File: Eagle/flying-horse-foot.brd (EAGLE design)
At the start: 55.8 x 32.5 mm, 20 parts, among them U1 8U2-AU, Y1 16MHz

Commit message: rel 1
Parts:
- added S1: MK6-5-B, switch-reed:MK6-5
- C4, C6: value 0.1uF -> 1.0uF
- C7, C8: value 1.0uF -> 0.1uF
- U$1, U$2: value 74HC42 -> 74HC42D16; device aaa2:SOIC127P1032X265-16N -> aaa2:D16
- moved RESET 36.1 mm to (42.5, 17.1), turned to 270 degrees
- moved C5 23.6 mm to (41.9, 25.4)
- moved C8 22.9 mm to (13.3, 30.7)
- moved C7 20.7 mm to (45.7, 1.91)
- moved C4 18.3 mm to (36.8, 21.0)
- moved C6 8.02 mm to (36.8, 30.9), turned to 180 degrees
- moved C2 4.58 mm to (41.8, 30.9), turned to 180 degrees
- moved C3 2.29 mm to (41.9, 28.6)
- moved R1 2.16 mm to (46.4, 22.6)
- moved R2 1.90 mm to (46.4, 24.8)
- moved U$1 1.80 mm to (45.7, 8.26)
- moved R5 1.65 mm to (4.45, 29.0)
- moved Y1 1.42 mm to (45.7, 29.8), turned to 90 degrees
- moved U$2 1.02 mm to (13.3, 24.4)
- moved C1 0.63 mm to (50.2, 29.2)
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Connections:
- removed net N$9: RESET.2, U1.24
- new net RESET: RESET.2, S1.1, U1.24
- net COL-3: no longer U$4.13
- net COL-5: now also U$4.13
- net GND: now also C5.1, C8.2, S1.2; no longer C5.2, C8.1
- net N$3: now also C2.1; no longer C3.1
- net N$4: now also C3.1; no longer C2.1
- net N$6: now also C4.1; no longer C7.1
- net VCC: now also C5.2, C7.1, C8.1; no longer C4.1, C5.1, C8.2
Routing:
- net VCC: track 0.00 -> 94.5 mm, vias 0 -> 4
- net ROW-A: track 0.00 -> 57.2 mm, vias 0 -> 2
- net ROW-B: track 0.00 -> 55.1 mm, vias 0 -> 2
- net ROW-C: track 0.00 -> 51.5 mm, vias 0 -> 2
- net ROW-D: track 0.00 -> 50.6 mm, vias 0 -> 2
- net ROW-5: track 0.00 -> 41.2 mm, vias 0 -> 2
- net ROW-18: track 0.00 -> 41.0 mm, vias 0 -> 2
- net COL-12: track 0.00 -> 40.6 mm, vias 0 -> 1
- net ROW-17: track 0.00 -> 39.6 mm
- net COL-6: track 0.00 -> 38.2 mm, vias 0 -> 1
- net COL-5: track 0.00 -> 36.3 mm, vias 0 -> 1
- net N$5: track 0.00 -> 32.5 mm, vias 0 -> 2
- net COL-4: track 0.00 -> 31.1 mm, vias 0 -> 1
- net COL-0: track 0.00 -> 29.8 mm, vias 0 -> 1
- net N$7: track 0.00 -> 28.7 mm, vias 0 -> 2
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- added copper zone on layer 1, net GND
- added copper zone on layer 16, net GND

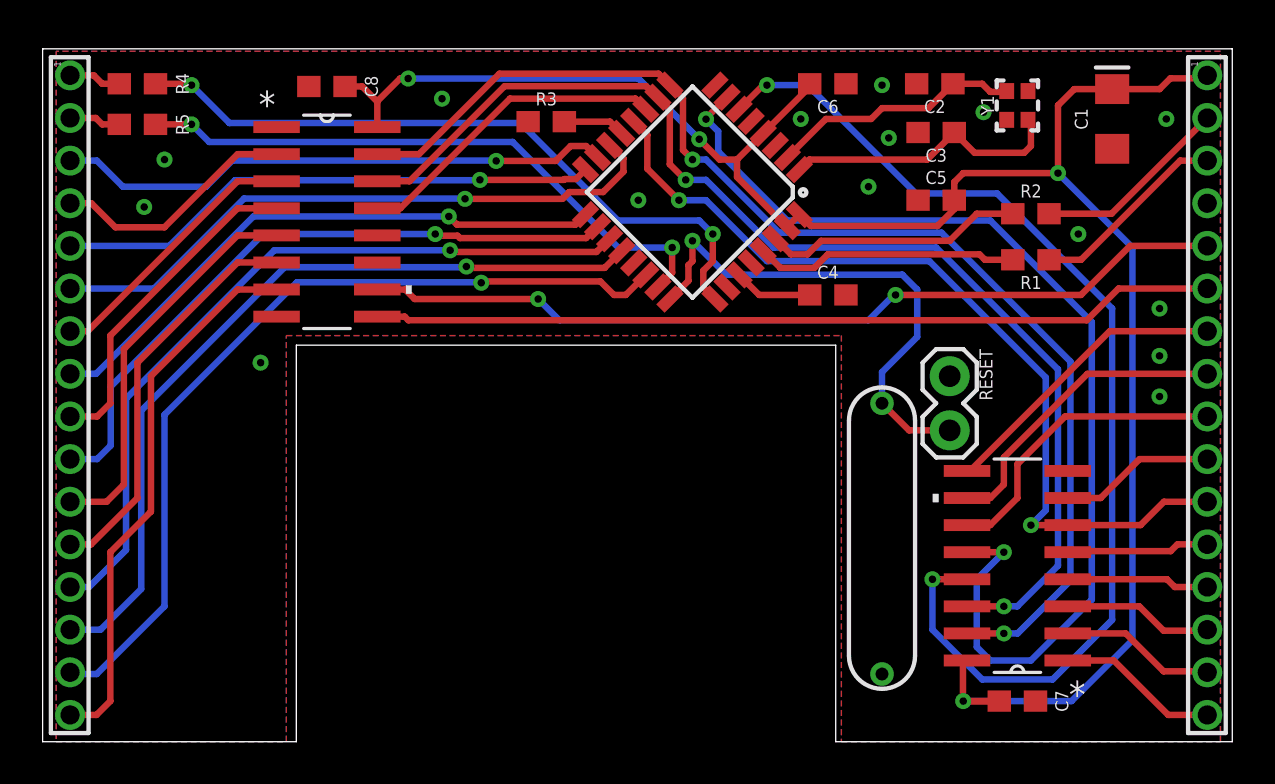
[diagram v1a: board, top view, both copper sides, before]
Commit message: made top plane vcc, instead of gnd
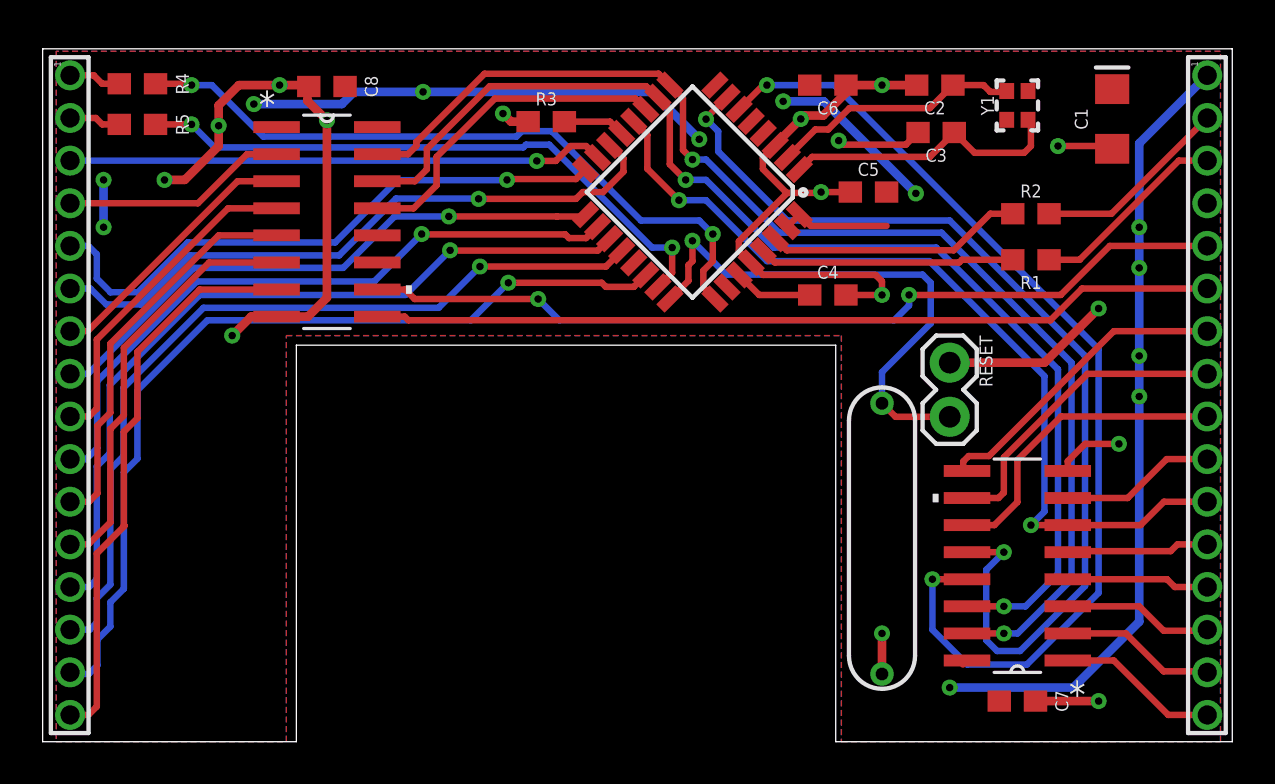
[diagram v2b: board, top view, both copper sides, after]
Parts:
- moved C5 3.20 mm to (38.7, 25.8)
- moved RESET 0.64 mm to (42.5, 17.8)
- moved C2 0.06 mm to (41.8, 30.8)
- moved C6 0.06 mm to (36.8, 30.8)
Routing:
- net GND: track 0.00 -> 76.6 mm, vias 15 -> 16
- net VCC: track 94.5 -> 75.2 mm, vias 4 -> 12
- net ROW-C: track 51.5 -> 47.8 mm
- net ROW-D: track 50.6 -> 47.5 mm
- net COL-2: track 25.7 -> 28.1 mm
- net COL-1: track 26.3 -> 25.3 mm
- net ROW-11: track 11.6 -> 10.6 mm
- net ROW-16: track 25.8 -> 26.6 mm
- net RESET: track 24.4 -> 25.2 mm
- net COL-12: track 40.6 -> 41.4 mm
- net ROW-E: track 14.9 -> 15.7 mm
- net ROW-B: track 55.1 -> 55.8 mm
- net COL-6: track 38.2 -> 39.0 mm
- net COL-5: track 36.3 -> 37.1 mm
- net ROW-15: track 18.9 -> 19.6 mm
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- added copper zone on layer 1, net VCC
- removed copper zone on layer 1, net GND

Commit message: prep for board manufacturing
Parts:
- removed Y1: 16MHz, SparkFun-Clocks:CRYSTAL-SMD-2.0X1.6MM
- added Y2: 16MHz, SparkFun-Clocks:CRYSTAL-SMD-5X3.2-4PAD
- C1: device SparkFun-Capacitors:EIA3216 -> aaa2:EEE-1CA100SR
- moved R1 1.48 mm to (45.1, 21.8)
- moved R2 1.48 mm to (45.1, 24.0)
- moved C5 1.05 mm to (39.0, 24.8)
- moved C1 0.85 mm to (49.8, 28.4), turned to 0 degrees
- moved C3 0.77 mm to (41.1, 28.4)
- moved C2 0.70 mm to (41.1, 30.7)
- moved C6 0.26 mm to (36.6, 30.7)
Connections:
- net N$3: now also Y2.3; no longer Y1.3
- net N$4: now also Y2.1; no longer Y1.1
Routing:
- net VCC: track 75.2 -> 68.1 mm, vias 12 -> 11
- net D-: track 9.28 -> 11.6 mm
- net GND: track 76.6 -> 74.4 mm, vias 16 -> 17
- net N$2: track 12.1 -> 10.5 mm
- net D+: track 9.35 -> 10.9 mm
- net N$1: track 12.0 -> 10.9 mm
- net N$3: track 11.8 -> 11.1 mm
- net ROW-D: track 47.5 -> 46.9 mm
- added copper zone on layer 1, net GND
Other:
- board text added: "5V"
- board text added: "74HC42"
- board text added: "A 8x18 switch matrix controller. All use is at your own risk. © 2015 Fredrik Atmer. Bathroom Epiphanies Inc."
- board text added: "ATMEGA32U2"
- board text added: "D+"
- board text added: "D-"
- board text added: "GND"
- board text added: "MISO"
- board text added: "MK6-5-B"
- board text added: "MOSI"
- board text added: "RESET"
- board text added: "Rev. 20210625 github.com/Tecsmith /flying-horse-foot"
- board text added: "SCLK"
- board text added: "The Pegasus Hoof"
- board text added: "bathroomepiphanies.com"

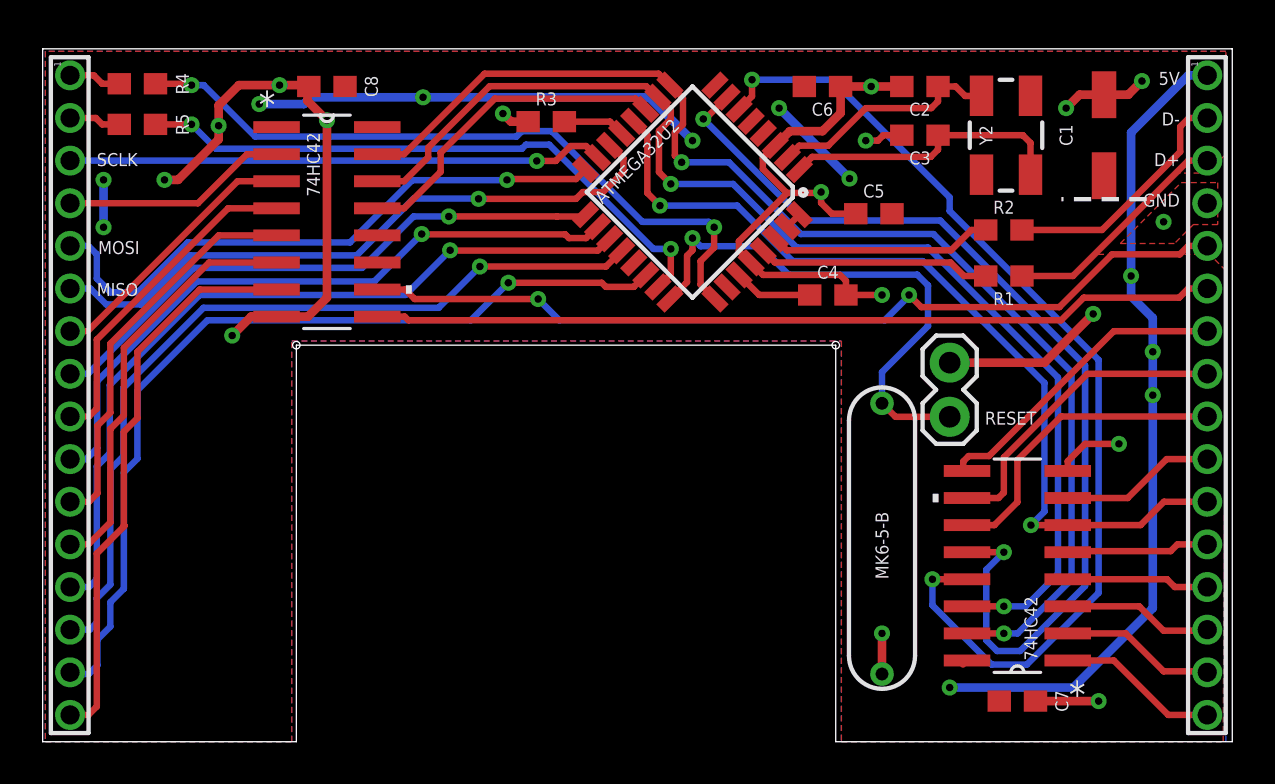
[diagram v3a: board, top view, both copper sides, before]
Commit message: Added SPI6 header for easier AVR programming
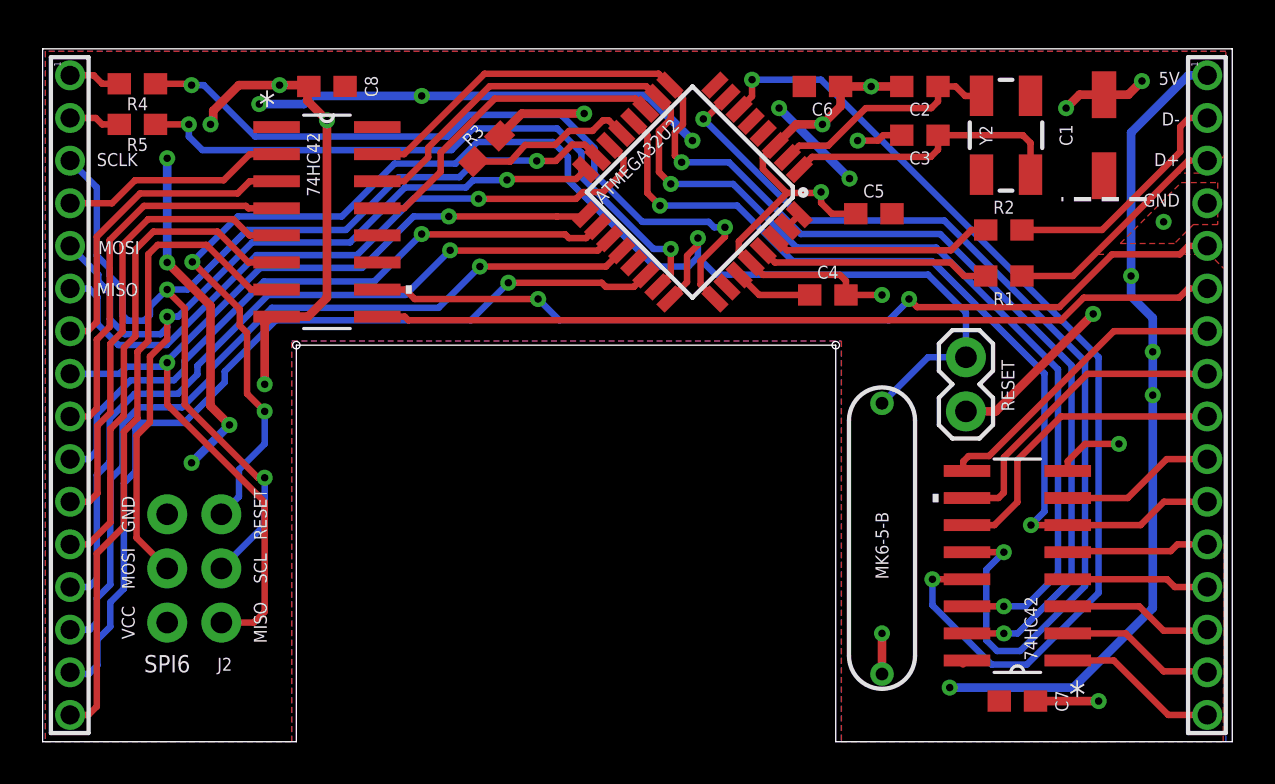
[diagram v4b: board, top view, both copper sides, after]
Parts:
- added J2: SPI6, SparkFun-Connectors:2X3-NS
- moved R3 3.07 mm to (20.8, 27.8), turned to 225 degrees
- moved RESET 2.41 mm to (43.3, 15.5), turned to 90 degrees
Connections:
- net COL-1: now also J2.3
- net COL-2: now also J2.4
- net COL-3: now also J2.1
- net GND: now also J2.6
- net RESET: now also J2.5
- net VCC: now also J2.2
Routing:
- net RESET: track 25.1 -> 68.2 mm, vias 1 -> 3
- net COL-1: track 25.3 -> 50.6 mm, vias 1 -> 3
- net COL-3: track 27.4 -> 43.3 mm, vias 1 -> 2
- net COL-2: track 28.1 -> 43.3 mm, vias 1 -> 2
- net VCC: track 68.1 -> 82.2 mm, vias 11 -> 13
- net HWB: track 2.92 -> 8.02 mm
- net ROW-16: track 26.6 -> 30.7 mm
- net ROW-15: track 19.6 -> 23.2 mm
- net ROW-14: track 18.6 -> 21.6 mm
- net ROW-13: track 15.6 -> 18.1 mm
- net ROW-12: track 12.6 -> 14.9 mm
- net COL-0: track 30.4 -> 32.7 mm
- net N$5: track 33.1 -> 35.2 mm
- net N$7: track 28.8 -> 30.5 mm
- net GND: track 74.4 -> 75.1 mm
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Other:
- board text added: "Rev. 20210625"
- board text added: "SCL"
- board text added: "SPI6"
- board text added: "VCC"
- board text added: "github.com/Tecsmith/flying-horse-foot"
- board text removed: "Rev. 20210625 github.com/Tecsmith /flying-horse-foot"

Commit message: Added jumper to disable magnetic reed switch
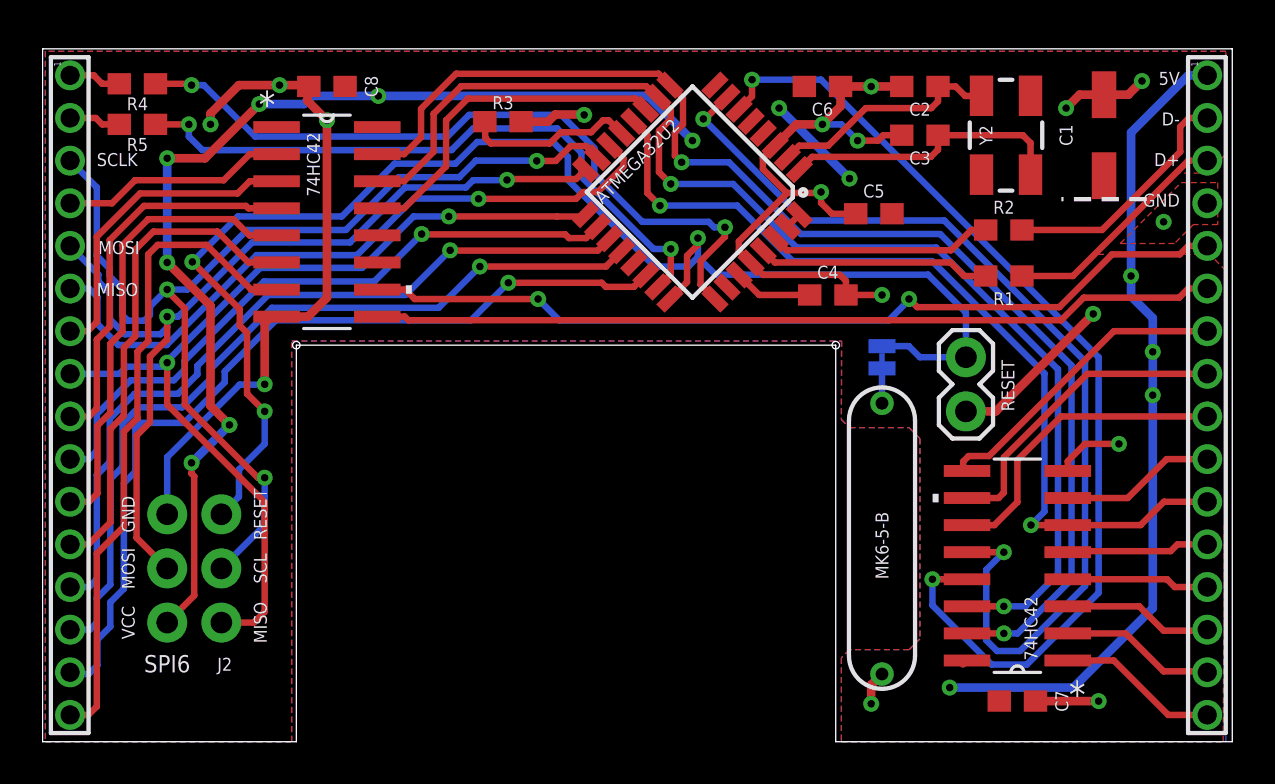
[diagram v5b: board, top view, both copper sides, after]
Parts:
- added JP1: Disable S1, SparkFun-Jumpers:SMT-JUMPER_2_NC_TRACE_NO-SILK
- moved R3 1.48 mm to (21.6, 29.1), turned to 180 degrees
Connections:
- new net N$8: JP1.1, S1.1
- net RESET: now also JP1.2; no longer S1.1
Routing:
- net VCC: track 82.2 -> 95.7 mm
- net GND: track 75.1 -> 84.1 mm
- net N$8: track 0.00 -> 1.64 mm
- net ROW-B: track 56.5 -> 57.3 mm
- net ROW-A: track 57.9 -> 58.7 mm
- net ROW-E: track 15.5 -> 16.2 mm
- net RESET: track 68.2 -> 67.6 mm

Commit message: first prototype exposed that the headers where over-wide by 0.34mm
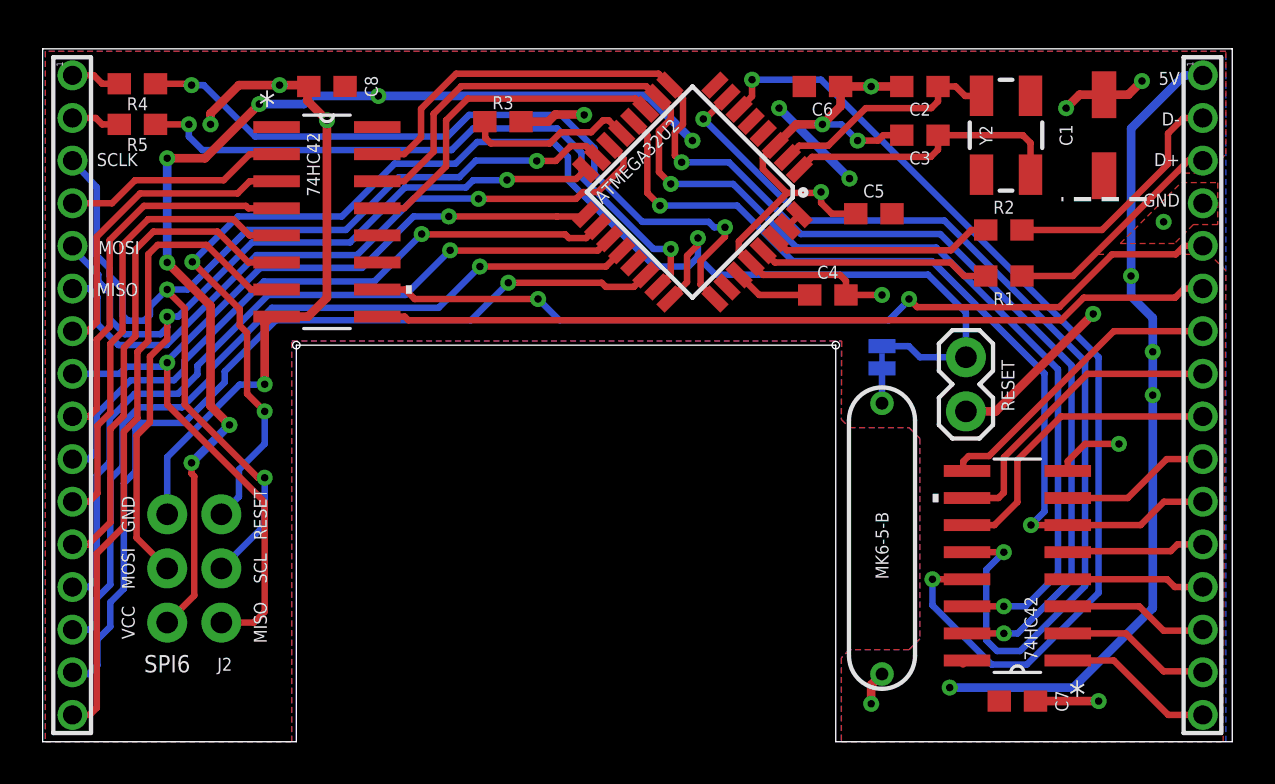
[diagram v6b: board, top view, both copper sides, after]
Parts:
- moved U$3 0.21 mm to (55.4, 16.3)
- moved U$4 0.11 mm to (2.40, 16.3)
